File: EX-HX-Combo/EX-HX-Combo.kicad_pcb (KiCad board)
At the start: 2 copper layers, 150.2 x 124.5 mm, 46 parts, among them CN1 DB9 Male, J1 IDE_CONNECTOR, J2 Bus_Tandy_Plus, J3 Bus_Tandy_Plus_Through, SW1 SW_DIP_x10, U1 BIOS FLASH, U2 74HCT245, U3 1.8432 MHz, U4 DS1315, U5 AS6C4008-55PCN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

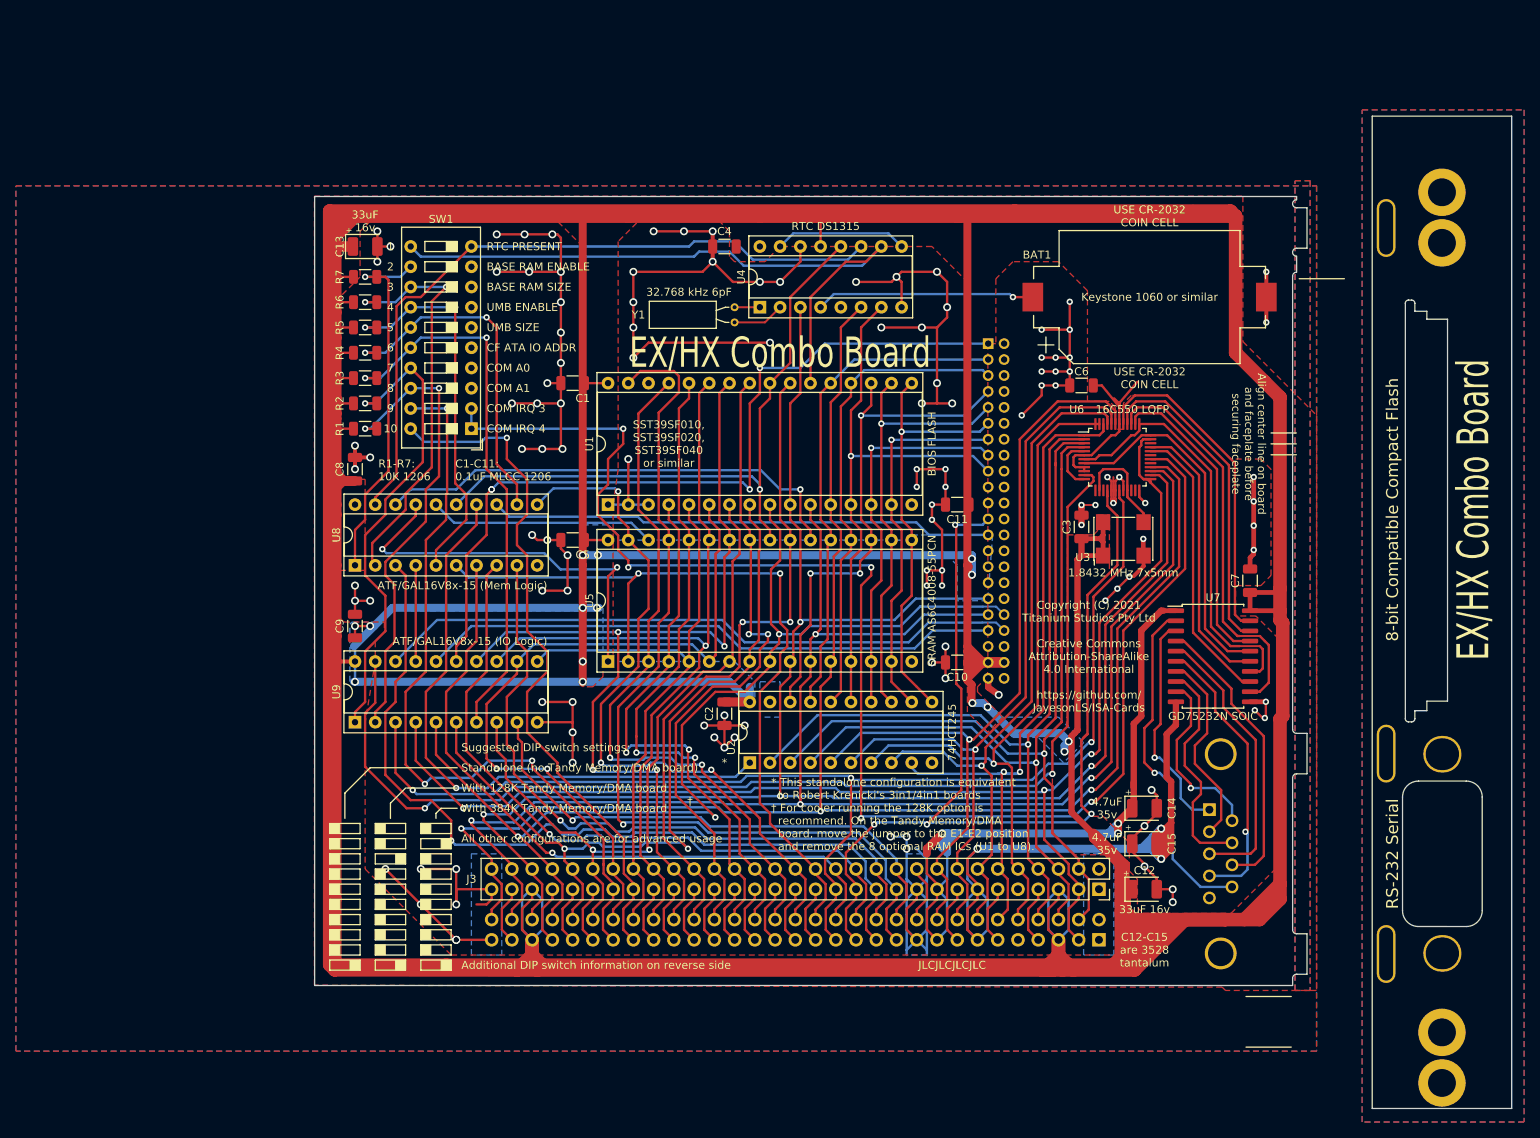
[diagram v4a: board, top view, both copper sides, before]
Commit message: EX-HX-Combo: Change jumper block setup. Remove COM port and IRQ options. Now fixed to COM1 and IRQ4. Add a jumper for V20+ processor.
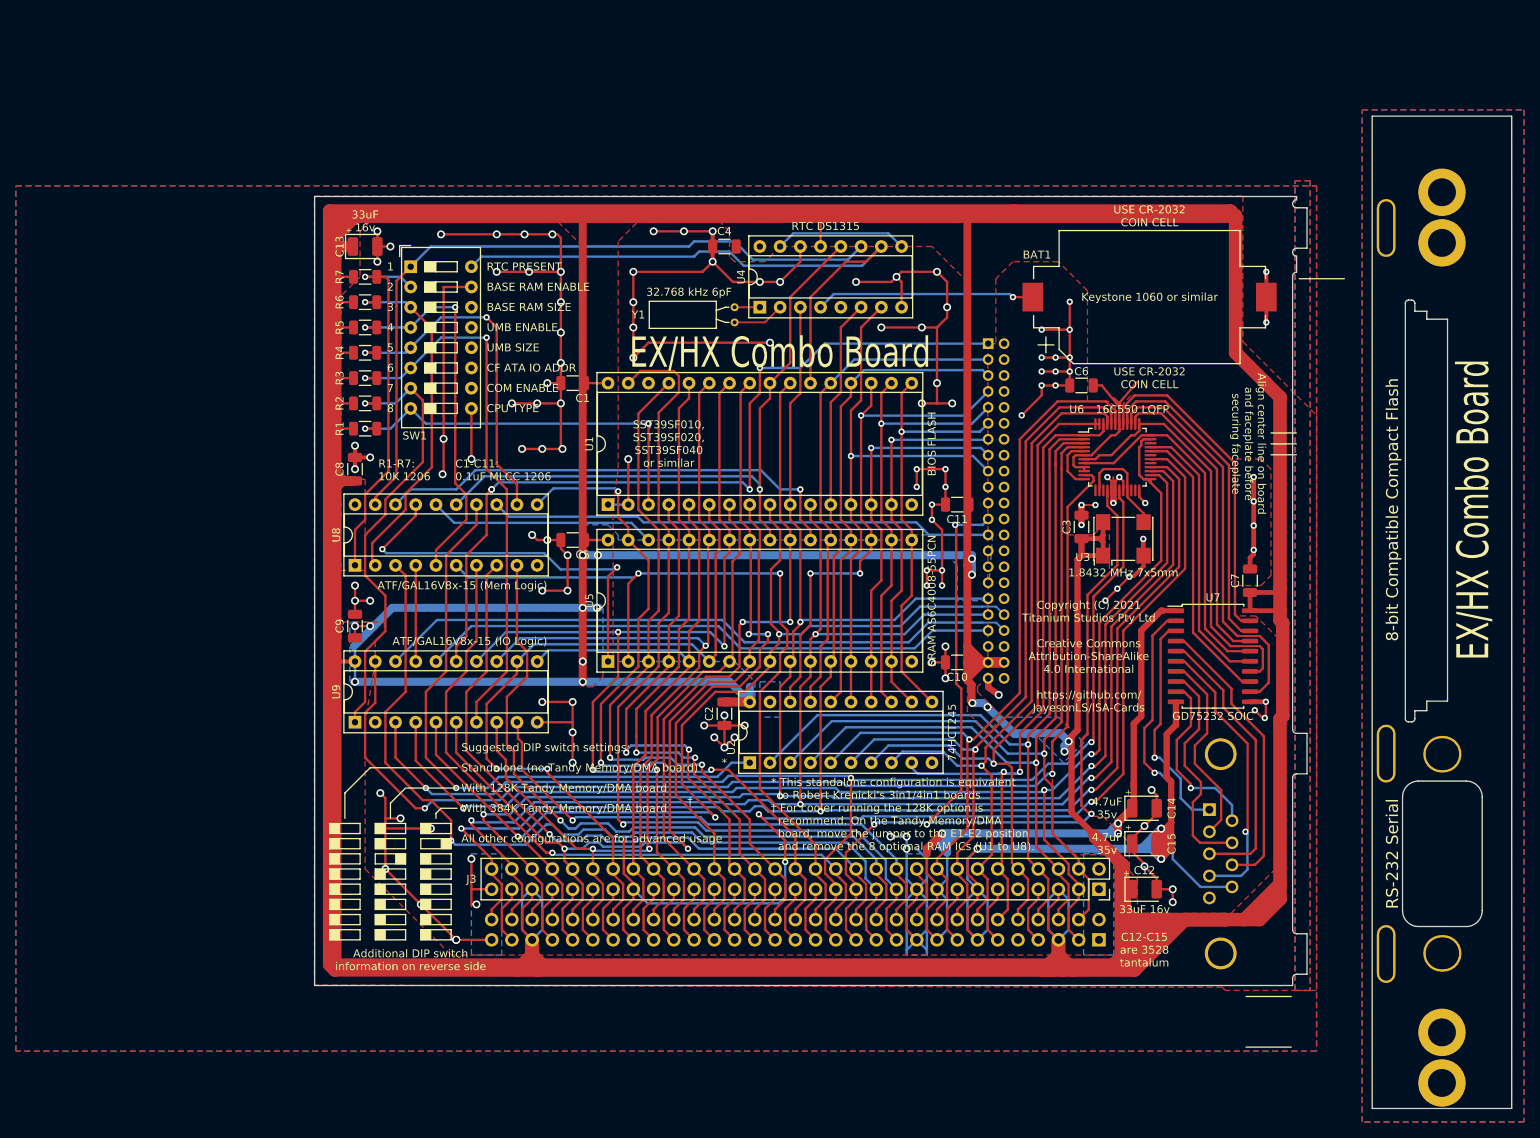
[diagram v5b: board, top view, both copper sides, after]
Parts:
- SW1: footprint Button_Switch_THT:SW_DIP_SPSTx10_Slide_9.78x27.58mm_W7.62mm_P2.54mm -> Button_Switch_THT:SW_DIP_SPSTx08_Slide_9.78x22.5mm_W7.62mm_P2.54mm
- U7: value GD75232N -> GD75232
- moved SW1 21.7 mm to (132.1, 46.4), turned to 0 degrees
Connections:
- R1 pad 2: UART_S1 -> CPU_TYPE
- R2 pad 2: UART_S0 -> UART_ENABLE
- SW1 pad 1: UART_IRQ -> ~CE~_BIOS_DECODE
- SW1 pad 10: ~CE~_BIOS_DECODE -> GND
- SW1 pad 11: ~CE~_BIOS_THRU -> GND
- SW1 pad 12: BASE_RAM_ENABLE -> GND
- SW1 pad 13: BASE_RAM_SIZE -> GND
- SW1 pad 14: UMB_ENABLE -> GND
- SW1 pad 15: UMB_SIZE -> GND
- SW1 pad 16: ATA_ADDR_JUMPER -> ~CE~_BIOS_THRU
- SW1 pad 2: UART_IRQ -> BASE_RAM_ENABLE
- SW1 pad 3: GND -> BASE_RAM_SIZE
- SW1 pad 4: GND -> UMB_ENABLE
- SW1 pad 5: GND -> UMB_SIZE
- SW1 pad 6: GND -> ATA_ADDR_JUMPER
- SW1 pad 7: GND -> UART_ENABLE
- SW1 pad 8: GND -> CPU_TYPE
- U1 pad 3: GND -> CPU_TYPE
- U6 pad 30: UART_IRQ -> IRQ4
- U9 pad 1: UART_S0 -> UART_ENABLE
- U9 pad 2: UART_S1 -> Net-(U9-Pad2)
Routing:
- net UART_IRQ: track 185.5 -> 0.00 mm, vias 5 -> 0
- net IRQ3: track 97.3 -> 7.40 mm, vias 3 -> 0
- net UART_S0: track 59.7 -> 0.00 mm, vias 1 -> 0
- net UART_S1: track 59.0 -> 0.00 mm, vias 2 -> 0
- net UART_ENABLE: track 0.00 -> 56.1 mm, vias 0 -> 1
- net IRQ4: track 86.7 -> 140.1 mm, vias 1 -> 3
- net CPU_TYPE: track 0.00 -> 49.0 mm, vias 0 -> 2
- net GND: track 460.5 -> 506.0 mm, vias 122 -> 128
- net ~CE~_BIOS_THRU: track 83.9 -> 76.3 mm
- net BASE_RAM_SIZE: track 51.3 -> 44.2 mm, vias 2 -> 1
- net ~CE~_BIOS_DECODE: track 89.3 -> 91.1 mm
- net A15: track 88.2 -> 89.5 mm
- net ~IOR: track 154.6 -> 153.5 mm
- net ~MEMR: track 108.6 -> 107.7 mm
- net ~UART_CS: track 145.0 -> 144.3 mm
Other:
- board text added: "8088/8086"
- board text added: "COM ENABLE"
- board text added: "COM1 Enable"
- board text added: "CPU TYPE"
- board text added: "CPU Type"
- board text added: "DIP Switches:"
- board text added: "V20, 286,..."
- board text removed: "COM"
- board text removed: "COM A0"
- board text removed: "COM A1"
- board text removed: "COM IRQ 3"
- board text removed: "COM IRQ 4"
- board text removed: "DIP Switches 1 to 6:"
- board text removed: "DIP Switches 7 to 10:"
- board text removed: "Suggested COM IRQ settings: COM1, COM3 -> IRQ4 COM2 -> IRQ3"

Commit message: EX-HX-Combo: Relocate back plate alignment tabs to very ends of boards. Also make them 1mm narrower. Remove middle alighment tab.
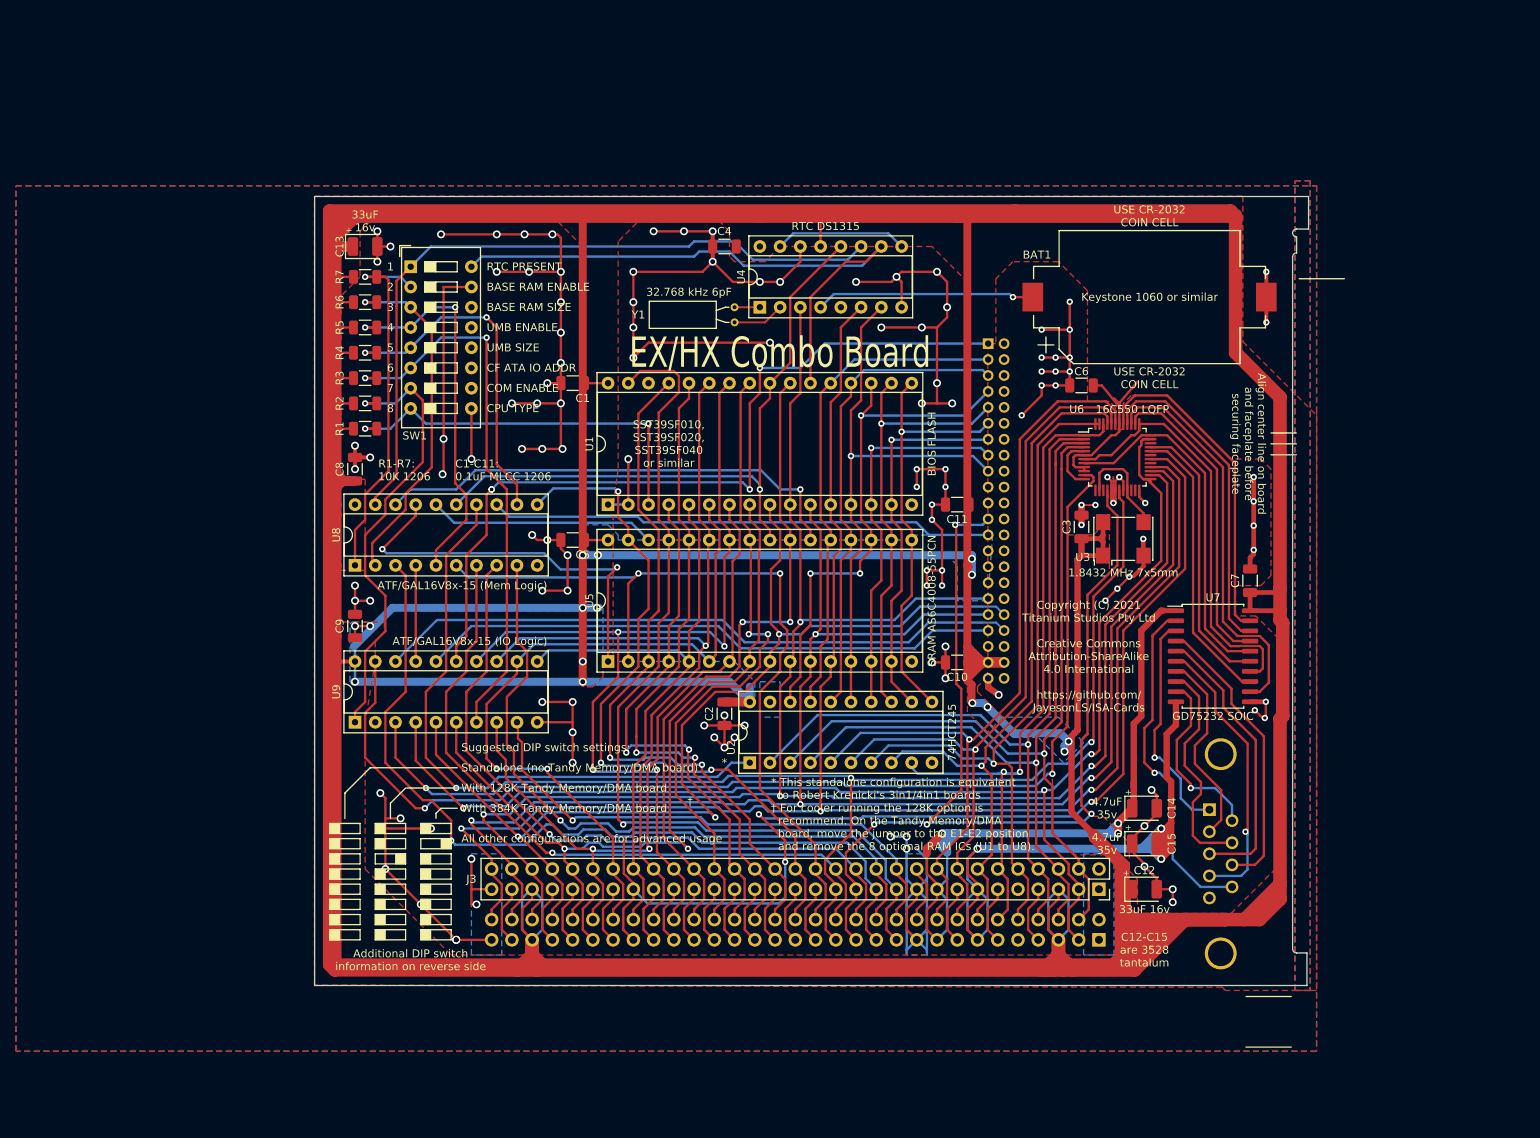
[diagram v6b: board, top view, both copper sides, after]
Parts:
- removed H1, H2, H3, H4: MountingHole_Pad, MountingHole:MountingHole_3.5mm_Pad
- removed H5, H6, H7: AlignmentHole_Pad, 00Custom:AlignmentHole
- removed H8: DB-9 Faceplate, 00Custom:DB9_Face
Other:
- board size 150.2 x 124.5 mm -> 124.7 x 99 mm
- board text removed: "8-bit Compatible Compact Flash"
- board text removed: "Copyright (C) 2021 Titanium Studios Pty Ltd Creative Commons Attribution-ShareAlike 4.0 International https://github.com/JayesonLS/ISA-Cards"
- board text removed: "RS-232 Serial"
- board text removed: "Where PCB aligns with bracket."

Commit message: EX-HX-Combo: Various refinements.
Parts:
- moved CN1 0.80 mm to (233.1, 114.5)
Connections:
- R1 pad 2: CPU_TYPE -> UART_ENABLE
- R2 pad 2: UART_ENABLE -> CPU_TYPE
- SW1 pad 7: UART_ENABLE -> CPU_TYPE
- SW1 pad 8: CPU_TYPE -> UART_ENABLE
- U1 pad 2: GND -> CPU_TYPE
- U1 pad 3: CPU_TYPE -> ATA_ADDR_JUMPER
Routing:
- net ATA_ADDR_JUMPER: track 69.7 -> 112.4 mm, vias 2 -> 3
- net GND: track 506.0 -> 512.6 mm
- net UART_ENABLE: track 56.1 -> 52.6 mm
- net CPU_TYPE: track 49.0 -> 46.7 mm
- net /SER_PIN7: track 28.4 -> 27.8 mm
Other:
- board size 124.7 x 99 mm -> 125.5 x 99 mm
- board text added: "8088"
- board text added: "BASE RAM DISABLE"
- board text added: "COM DISABLE"
- board text added: "EX/HX Combo"
- board text added: "RTC ABSENT"
- board text added: "UMB DISABLE"
- board text added: "V20"
- board text removed: "10"
- board text removed: "8088/8086"
- board text removed: "9"
- board text removed: "BASE RAM ENABLE"
- board text removed: "COM ENABLE"
- board text removed: "COM IRQ"
- board text removed: "COM/Serial Port"
- board text removed: "COM1 Enable"
- board text removed: "COM2"
- board text removed: "COM3"
- board text removed: "EX/HX Combo Board"
- board text removed: "IRQ3"
- board text removed: "IRQ4"
- board text removed: "Invalid"
- board text removed: "None"
- board text removed: "RTC PRESENT"
- board text removed: "UMB ENABLE"
- board text removed: "V20, 286,..."
- board text removed: "disabled or absent"

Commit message: EX-HX-Combo: Update GAL logic to match current board design.
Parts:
- U8: value GAL16V8 -> ATF/GAL16V8x-15 (Mem Logic)
- U9: value GAL16V8 -> ATF/GAL16V8x-15 (IO Logic)
